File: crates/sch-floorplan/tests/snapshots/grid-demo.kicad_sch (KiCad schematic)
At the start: 10 parts, among them U1 NE555P

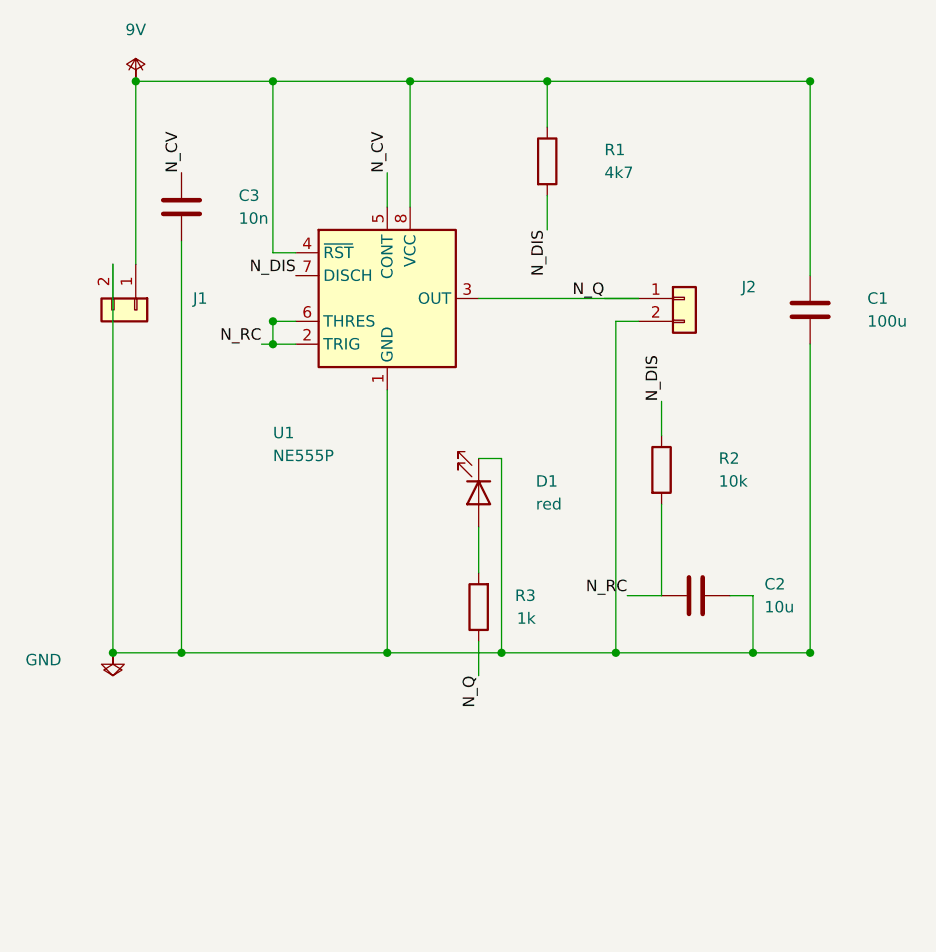
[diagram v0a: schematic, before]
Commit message: Bless grid-demo after the density trim (critic within noise)
Claude-Session: https://claude.ai/code/session_01GyGRY43X8yBh8WS1tjEmFz
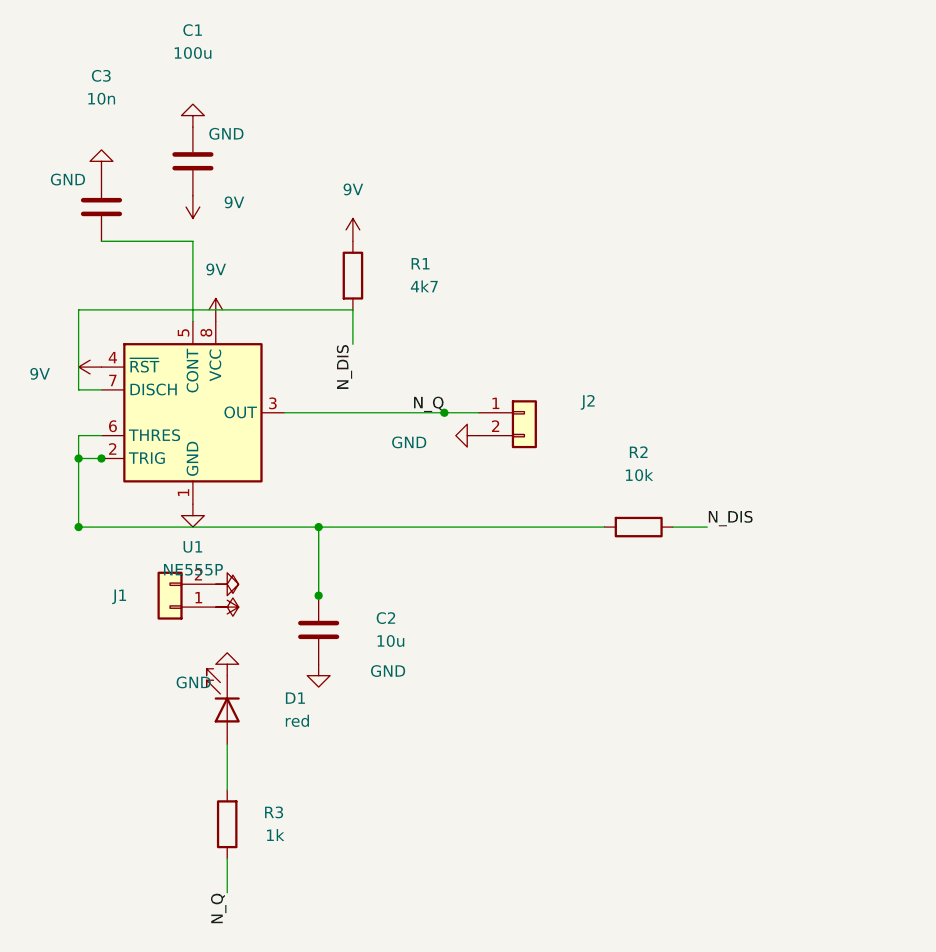
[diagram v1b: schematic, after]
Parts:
- C1, J1: ap_block (none) -> input
- C2, C3, R1, R2, U1: ap_block (none) -> blinker
- D1, J2, R3: ap_block (none) -> output
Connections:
- net N_CV: no longer names the net of C3.1, U1.5 (CONT)
- net N_RC: no longer names the net of C2.1, R2.2, U1.2 (TRIG), U1.6 (THRES)
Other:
- moved on the sheet: C1, C2, C3, D1, J1, J2, R1, R2, R3, U1
